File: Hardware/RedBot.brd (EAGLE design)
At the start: 94 x 49.5 mm, 40 parts, among them U1 ATMEGA328P, U2 TB6612FNG, U3 MIC5219 5V

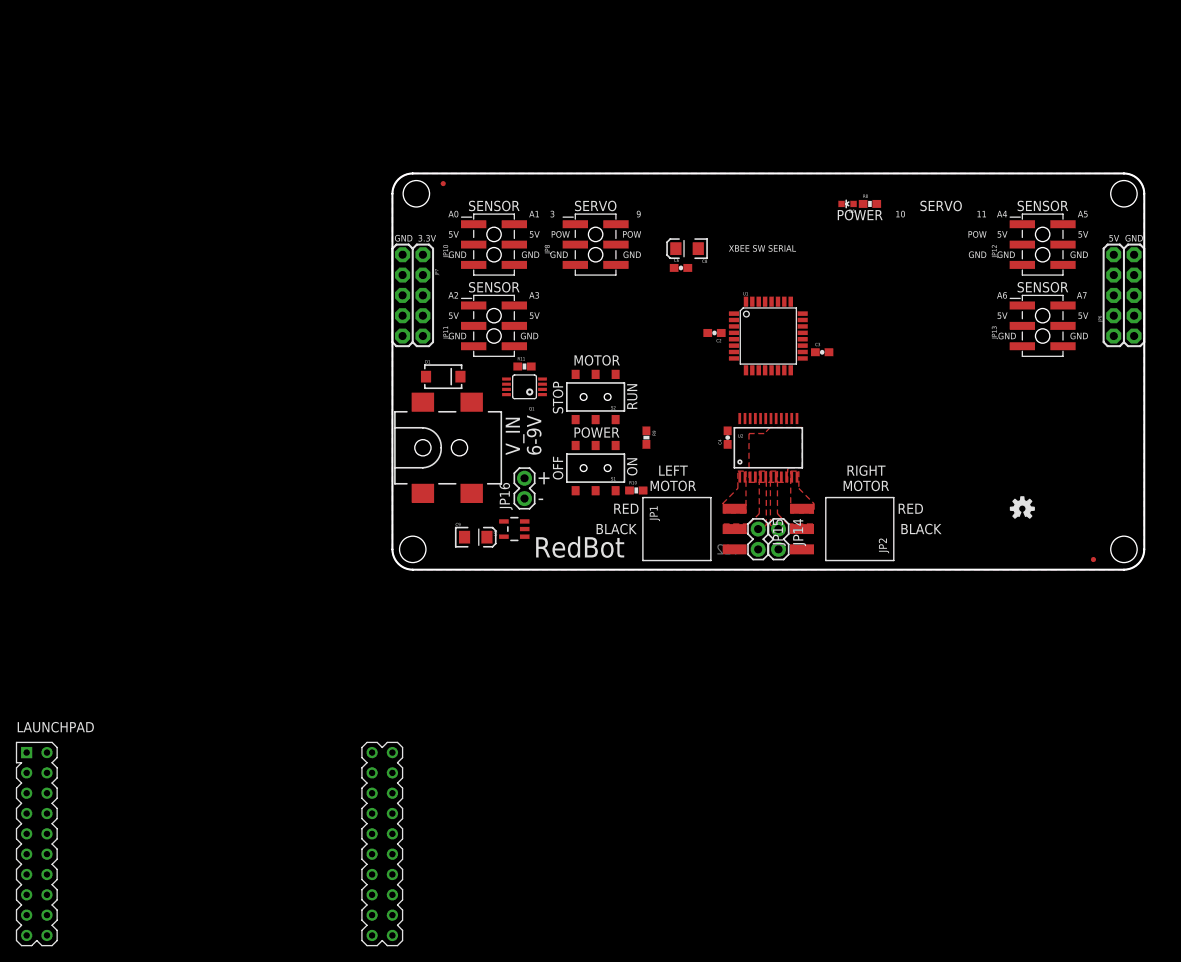
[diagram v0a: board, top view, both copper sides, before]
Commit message: Updated motor ic to use 3.3V
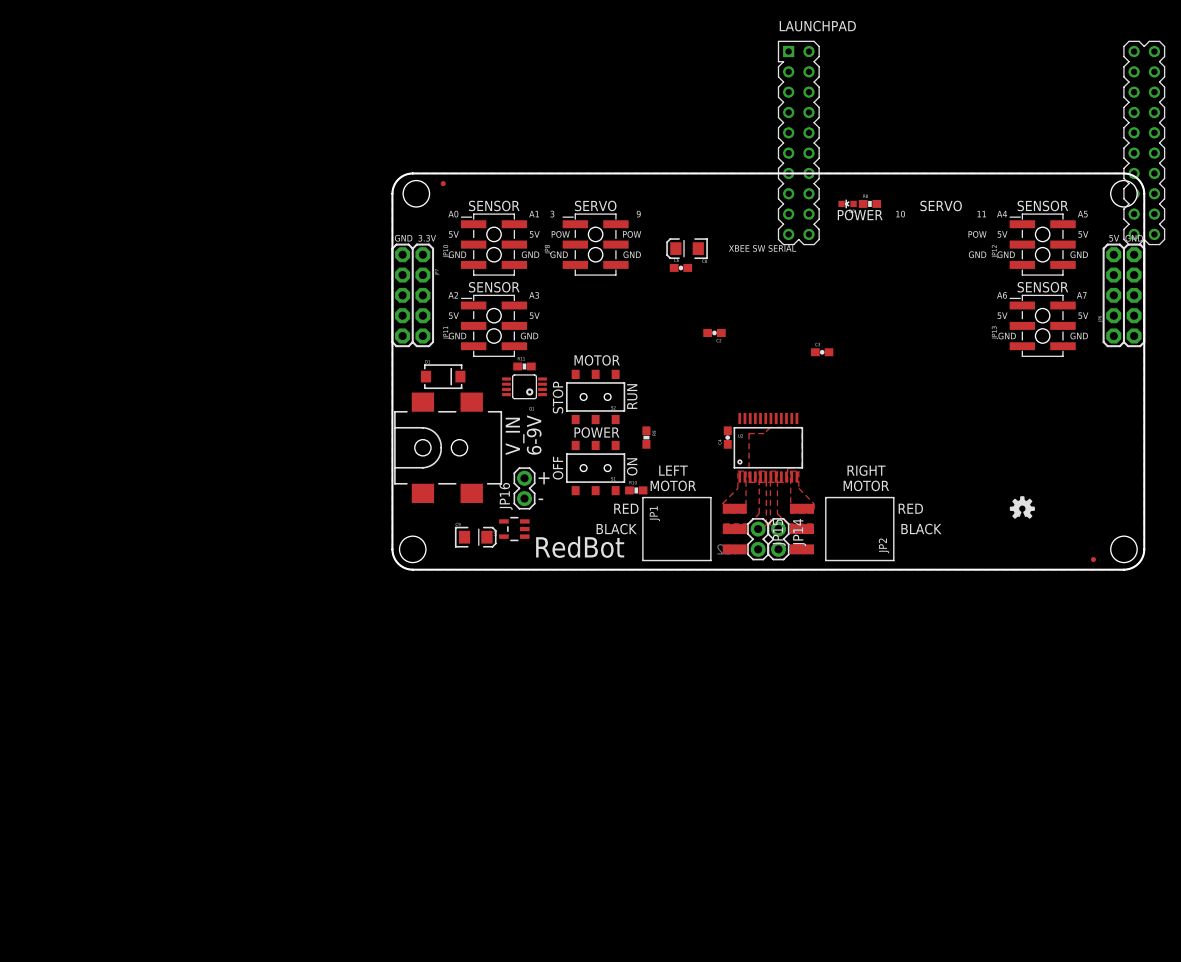
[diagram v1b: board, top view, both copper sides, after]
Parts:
- removed U1: ATMEGA328P, SparkFun-DigitalIC:TQFP32-08
- moved LAUNCHPAD 129.4 mm to (72.4, 53.3)
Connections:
- removed net MISO: U1.16
- removed net SCK: U1.17
- removed net SERVO_4/MOSI: U1.15
- net 3.3V: now also U2.20
- net 5V: no longer U2.20
- net L_CTRL_2: no longer U1.2
- net SERVO_1: no longer U1.1
- net SERVO_2: no longer U1.13
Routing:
- net MISO: track 5.26 -> 0.00 mm
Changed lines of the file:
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@@
 <elements>
 <element name="FRAME1" library="SparkFun-Aesthetics" package="CREATIVE_COMMONS" value="FRAME-LETTER" x="-26.67" y="-16.51"/>
-<element name="U1" library="SparkFun-DigitalIC" package="TQFP32-08" value="ATMEGA328P" x="46.99" y="29.21">
-<attribute name="PROD_ID" value="IC-09069" x="109.22" y="-13.97" size="1.778" layer="27" display="off"/>
-<attribute name="VALUE" value="ATMEGA328P" x="109.22" y="-13.97" size="1.778" layer="27" display="off"/>
-</element>
 <element name="C2" library="SparkFun-Capacitors" package="0603-CAP" value="0.1uF" x="40.259" y="29.591" rot="R180">
 <attribute name="PROD_ID" value="CAP-00810" x="-14.351" y="101.981" size="1.778" layer="27" rot="R180" display="off"/>
@@
 <element name="FID1" library="SparkFun-Aesthetics" package="MICRO-FIDUCIAL" value="FIDUCIALUFIDUCIAL" x="6.35" y="48.26"/>
 <element name="FID2" library="SparkFun-Aesthetics" package="MICRO-FIDUCIAL" value="FIDUCIALUFIDUCIAL" x="87.63" y="1.27"/>
-<element name="LAUNCHPAD" library="zlalanne" package="BOOSTERPACK40" value="BOOSTERPACK" x="-22.86" y="-34.29"/>
+<element name="LAUNCHPAD" library="zlalanne" package="BOOSTERPACK40" value="BOOSTERPACK" x="72.39" y="53.34"/>
 </elements>
 <signals>
@@
 <wire x1="9.014" y1="4.064" x2="9.91" y2="9.54" width="0" layer="19" extent="1-1"/>
 <wire x1="3.81" y1="9.54" x2="9.91" y2="9.54" width="0" layer="19" extent="1-1"/>
-<wire x1="0" y1="-22.86" x2="9.014" y2="4.064" width="0" layer="19" extent="1-1"/>
-<wire x1="-43.18" y1="-25.4" x2="0" y2="-22.86" width="0" layer="19" extent="1-1"/>
+<wire x1="95.25" y1="64.77" x2="9.014" y2="4.064" width="0" layer="19" extent="1-1"/>
+<wire x1="52.07" y1="62.23" x2="95.25" y2="64.77" width="0" layer="19" extent="1-1"/>
 </signal>
 <signal name="SENSOR_0">
@@
 <wire x1="7.493" y1="40.386" x2="7.493" y2="43.18" width="0.254" layer="2"/>
 <contactref element="LAUNCHPAD" pad="23"/>
-<wire x1="11.049" y1="36.83" x2="-43.18" y2="-27.94" width="0" layer="19" extent="1-2"/>
+<wire x1="11.049" y1="36.83" x2="52.07" y2="59.69" width="0" layer="19" extent="1-2"/>
 <wire x1="10.16" y1="43.18" x2="7.493" y2="43.18" width="0" layer="19" extent="1-2"/>
 </signal>
@@
 <wire x1="7.62" y1="33.782" x2="7.62" y2="33.02" width="0.254" layer="2"/>
 <contactref element="LAUNCHPAD" pad="25"/>
-<wire x1="7.62" y1="33.02" x2="-43.18" y2="-33.02" width="0" layer="19" extent="1-2"/>
+<wire x1="7.62" y1="33.02" x2="52.07" y2="54.61" width="0" layer="19" extent="1-2"/>
 <wire x1="10.16" y1="33.02" x2="8.382" y2="34.544" width="0" layer="19" extent="1-2"/>
 </signal>
@@
 <wire x1="18.288" y1="32.512" x2="17.78" y2="33.02" width="0.254" layer="2"/>
 <contactref element="LAUNCHPAD" pad="26"/>
-<wire x1="15.24" y1="33.02" x2="-43.18" y2="-35.56" width="0" layer="19" extent="1-1"/>
+<wire x1="15.24" y1="33.02" x2="52.07" y2="52.07" width="0" layer="19" extent="1-1"/>
 <wire x1="17.78" y1="33.02" x2="15.24" y2="33.02" width="0" layer="19" extent="1-2"/>
 </signal>
@@
 <contactref element="JP12" pad="1"/>
 <contactref element="LAUNCHPAD" pad="27"/>
-<wire x1="-43.18" y1="-38.1" x2="78.74" y2="43.18" width="0" layer="19" extent="1-1"/>
+<wire x1="52.07" y1="49.53" x2="78.74" y2="43.18" width="0" layer="19" extent="1-1"/>
 </signal>
 <signal name="SENSOR_5">
 <contactref element="JP12" pad="2"/>
 <contactref element="LAUNCHPAD" pad="28"/>
-<wire x1="-43.18" y1="-40.64" x2="83.82" y2="43.18" width="0" layer="19" extent="1-1"/>
+<wire x1="52.07" y1="46.99" x2="83.82" y2="43.18" width="0" layer="19" extent="1-1"/>
 </signal>
 <signal name="SENSOR_6">
 <contactref element="JP13" pad="1"/>
 <contactref element="LAUNCHPAD" pad="2"/>
-<wire x1="-45.72" y1="-25.4" x2="78.74" y2="33.02" width="0" layer="19" extent="1-1"/>
+<wire x1="49.53" y1="62.23" x2="78.74" y2="33.02" width="0" layer="19" extent="1-1"/>
 </signal>
 <signal name="SENSOR_7">
 <contactref element="JP13" pad="2"/>
 <contactref element="LAUNCHPAD" pad="6"/>
-<wire x1="-45.72" y1="-35.56" x2="83.82" y2="33.02" width="0" layer="19" extent="1-1"/>
+<wire x1="49.53" y1="52.07" x2="83.82" y2="33.02" width="0" layer="19" extent="1-1"/>
 </signal>
 <signal name="SERVO_1">
-<contactref element="U1" pad="1"/>
 <contactref element="JP8" pad="1"/>
 <contactref element="LAUNCHPAD" pad="38"/>
-<wire x1="22.86" y1="43.18" x2="42.6974" y2="32.01" width="0" layer="19" extent="1-1"/>
-<wire x1="-2.54" y1="-27.94" x2="42.6974" y2="32.01" width="0" layer="19" extent="1-1"/>
+<wire x1="22.86" y1="43.18" x2="92.71" y2="59.69" width="0" layer="19" extent="1-1"/>
 </signal>
 <signal name="PWML">
@@
 </signal>
 <signal name="SERVO_2">
-<contactref element="U1" pad="13"/>
 <contactref element="JP8" pad="2"/>
 <contactref element="LAUNCHPAD" pad="37"/>
-<wire x1="47.39" y1="24.9174" x2="27.94" y2="43.18" width="0" layer="19" extent="1-1"/>
-<wire x1="-2.54" y1="-30.48" x2="47.39" y2="24.9174" width="0" layer="19" extent="1-1"/>
-</signal>
-<signal name="SERVO_4/MOSI">
-<contactref element="U1" pad="15"/>
-</signal>
-<signal name="MISO">
-<contactref element="U1" pad="16"/>
-<wire x1="59.182" y1="23.749" x2="62.103" y2="23.749" width="0.254" layer="2"/>
-<wire x1="62.103" y1="23.749" x2="63.754" y2="25.4" width="0.254" layer="2"/>
-<wire x1="49.79" y1="24.9174" x2="59.182" y2="23.749" width="0" layer="19" extent="1-2"/>
-</signal>
-<signal name="SCK">
-<contactref element="U1" pad="17"/>
+<wire x1="27.94" y1="43.18" x2="92.71" y2="57.15" width="0" layer="19" extent="1-1"/>
 </signal>
 <signal name="5V">
 <contactref element="U3" pad="5"/>
-<contactref element="U2" pad="20"/>
 <contactref element="R8" pad="2"/>
 <contactref element="C9" pad="A"/>
@@
 <wire x1="60.54" y1="45.72" x2="90.17" y2="39.37" width="0" layer="19" extent="1-1"/>
 <wire x1="52.871" y1="27.178" x2="60.54" y2="45.72" width="0" layer="19" extent="1-1"/>
-<wire x1="46.015" y1="18.896" x2="52.871" y2="27.178" width="0" layer="19" extent="1-1"/>
-<wire x1="41.91" y1="15.66" x2="46.015" y2="18.896" width="0" layer="19" extent="1-1"/>
-<wire x1="41.109" y1="29.591" x2="46.015" y2="18.896" width="0" layer="19" extent="1-1"/>
+<wire x1="41.109" y1="29.591" x2="52.871" y2="27.178" width="0" layer="19" extent="1-1"/>
+<wire x1="41.91" y1="15.66" x2="41.109" y2="29.591" width="0" layer="19" extent="1-1"/>
+<wire x1="52.07" y1="64.77" x2="60.54" y2="45.72" width="0" layer="19" extent="1-1"/>
 <wire x1="13.9399" y1="4.13" x2="41.91" y2="15.66" width="0" layer="19" extent="1-1"/>
 <wire x1="11.814" y1="4.064" x2="13.9399" y2="4.13" width="0" layer="19" extent="1-1"/>
-<wire x1="-43.18" y1="-22.86" x2="11.814" y2="4.064" width="0" layer="19" extent="1-1"/>
 </signal>
 <signal name="PROGRAM_ENABLE">
@@
 <signal name="L_CTRL_2">
 <contactref element="U2" pad="22"/>
-<contactref element="U1" pad="2"/>
 <contactref element="LAUNCHPAD" pad="33"/>
-<wire x1="44.715" y1="18.896" x2="42.6974" y2="31.21" width="0" layer="19" extent="1-1"/>
-<wire x1="-2.54" y1="-40.64" x2="44.715" y2="18.896" width="0" layer="19" extent="1-1"/>
+<wire x1="44.715" y1="18.896" x2="92.71" y2="46.99" width="0" layer="19" extent="1-1"/>
 </signal>
 <signal name="L_CTRL_1">
 <contactref element="U2" pad="21"/>
 <contactref element="LAUNCHPAD" pad="34"/>
-<wire x1="-2.54" y1="-38.1" x2="45.365" y2="18.896" width="0" layer="19" extent="1-1"/>
+<wire x1="92.71" y1="49.53" x2="45.365" y2="18.896" width="0" layer="19" extent="1-1"/>
 </signal>
 <signal name="R_CTRL_1">
 <contactref element="U2" pad="17"/>
 <contactref element="LAUNCHPAD" pad="32"/>
-<wire x1="-2.54" y1="-43.18" x2="47.965" y2="18.896" width="0" layer="19" extent="1-1"/>
+<wire x1="92.71" y1="44.45" x2="47.965" y2="18.896" width="0" layer="19" extent="1-1"/>
 </signal>
 <signal name="R_CTRL_2">
 <contactref element="U2" pad="16"/>
 <contactref element="LAUNCHPAD" pad="31"/>
-<wire x1="-2.54" y1="-45.72" x2="48.615" y2="18.896" width="0" layer="19" extent="1-1"/>
+<wire x1="92.71" y1="41.91" x2="48.615" y2="18.896" width="0" layer="19" extent="1-1"/>
 </signal>
 <signal name="L01">
@@
 <contactref element="JP7" pad="3"/>
 <contactref element="JP7" pad="1"/>
+<contactref element="U2" pad="20"/>
 <wire x1="78.74" y1="40.64" x2="83.82" y2="40.64" width="0" layer="19" extent="1-1"/>
 <wire x1="83.82" y1="30.48" x2="83.82" y2="40.64" width="0" layer="19" extent="1-1"/>
 <wire x1="78.74" y1="30.48" x2="83.82" y2="30.48" width="0" layer="19" extent="1-1"/>
-<wire x1="35.43" y1="40.132" x2="78.74" y2="40.64" width="0" layer="19" extent="1-1"/>
-<wire x1="35.218" y1="37.719" x2="35.43" y2="40.132" width="0" layer="19" extent="1-1"/>
-<wire x1="15.24" y1="40.64" x2="35.43" y2="40.132" width="0" layer="19" extent="1-1"/>
+<wire x1="46.015" y1="18.896" x2="78.74" y2="30.48" width="0" layer="19" extent="1-1"/>
+<wire x1="35.218" y1="37.719" x2="46.015" y2="18.896" width="0" layer="19" extent="1-1"/>
+<wire x1="35.43" y1="40.132" x2="35.218" y2="37.719" width="0" layer="19" extent="1-1"/>
+<wire x1="15.24" y1="40.64" x2="35.218" y2="37.719" width="0" layer="19" extent="1-1"/>
 <wire x1="10.16" y1="40.64" x2="15.24" y2="40.64" width="0" layer="19" extent="1-1"/>
 <wire x1="3.81" y1="39.37" x2="10.16" y2="40.64" width="0" layer="19" extent="1-1"/>
@@
 <wire x1="10.16" y1="30.48" x2="3.81" y2="31.75" width="0" layer="19" extent="1-1"/>
 <wire x1="15.24" y1="30.48" x2="10.16" y2="30.48" width="0" layer="19" extent="1-1"/>
-<wire x1="-45.72" y1="-22.86" x2="3.81" y2="29.21" width="0" layer="19" extent="1-1"/>
+<wire x1="49.53" y1="64.77" x2="35.43" y2="40.132" width="0" layer="19" extent="1-1"/>
 </signal>
 <signal name="N$8">
@@
 <wire x1="19.05" y1="44.45" x2="17.78" y2="43.18" width="0.254" layer="15"/>
 <contactref element="LAUNCHPAD" pad="24"/>
-<wire x1="15.24" y1="43.18" x2="-43.18" y2="-30.48" width="0" layer="19" extent="1-1"/>
+<wire x1="15.24" y1="43.18" x2="52.07" y2="57.15" width="0" layer="19" extent="1-1"/>
 <wire x1="17.78" y1="43.18" x2="15.24" y2="43.18" width="0" layer="19" extent="1-15"/>
 </signal>

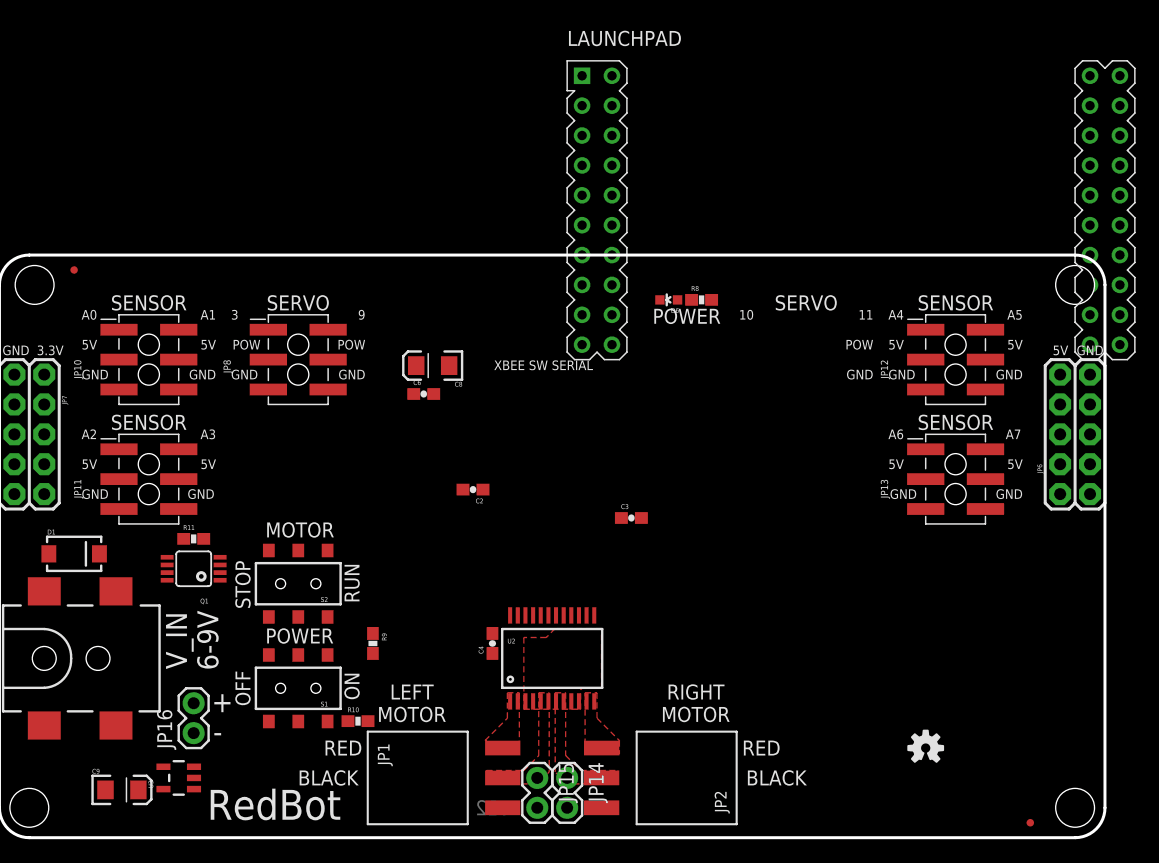
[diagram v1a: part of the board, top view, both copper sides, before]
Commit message: Updated parts to use through hole for sensor/servo connectors
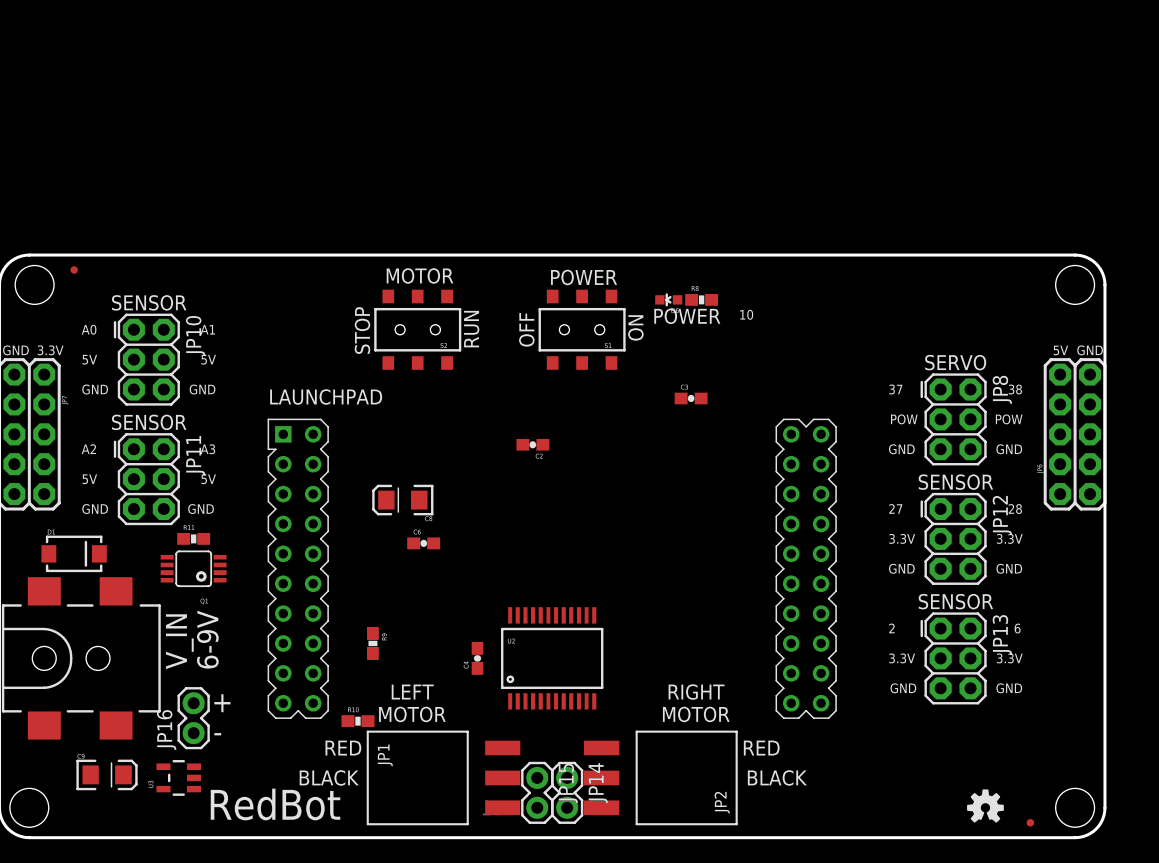
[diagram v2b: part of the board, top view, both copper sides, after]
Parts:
- JP10, JP11, JP12, JP13, JP8: device SparkFun-Connectors:2X3_SMT_POSTS -> SparkFun-Connectors:2X3
- moved JP8 54.7 mm to (80.0, 38.1)
- moved LAUNCHPAD 39.7 mm to (47.0, 22.9)
- moved S1 38.9 mm to (49.5, 43.2)
- moved FRAME1 37.5 mm to (6.35, 1.27)
- moved S2 23.9 mm to (35.6, 43.2)
- moved JP12 12.8 mm to (80.0, 27.9)
- moved JP13 12.8 mm to (80.0, 17.8)
- moved C6 12.7 mm to (36.1, 25.0)
- moved C8 11.7 mm to (34.3, 28.7)
- moved C3 11.4 mm to (58.8, 37.3)
- moved U$17 7.18 mm to (83.8, 2.54)
- moved C2 6.35 mm to (45.3, 33.4)
- moved JP11 2.84 mm to (11.4, 33.0)
- moved JP10 2.84 mm to (11.4, 43.2)
- moved C9 1.80 mm to (9.14, 5.33)
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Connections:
- net 3.3V: now also C4.1
- net 5V: no longer C4.1
- net SERVO_1: now also LAUNCHPAD.37; no longer LAUNCHPAD.38
- net SERVO_2: now also LAUNCHPAD.38; no longer LAUNCHPAD.37
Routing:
- net V_GATED: track 100.1 -> 0.00 mm
- net V_IN: track 98.0 -> 0.00 mm
- net V_BATT: track 66.1 -> 0.00 mm
- net SENSOR_0: track 51.1 -> 0.00 mm
- net SENSOR_2: track 42.6 -> 0.00 mm
- net SENSOR_3: track 35.5 -> 0.00 mm
- net MOTOR_ENABLE: track 29.2 -> 0.00 mm
- net SENSOR_1: track 26.2 -> 0.00 mm
- net PWMR: track 2.57 -> 0.00 mm
- removed copper zone on layer 2, net 5V
- removed copper zone on layer 15, net GND
- removed copper zone on layer 1, net L01
- removed copper zone on layer 1, net L02
- removed copper zone on layer 1, net R01
- removed copper zone on layer 1, net R02
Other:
- board text added: "2"
- board text added: "27"
- board text added: "28"
- board text added: "37"
- board text added: "38"
- board text added: "6"
- board text added: "v1"
- board text removed: "11"
- board text removed: "3"
- board text removed: "9"
- board text removed: "A4"
- board text removed: "A5"
- board text removed: "A6"
- board text removed: "A7"
- board text removed: "M. Hord"
- board text removed: "XBEE SW SERIAL"
- board text removed: "sparkfun.com/redbot"
- board text removed: "v12"
